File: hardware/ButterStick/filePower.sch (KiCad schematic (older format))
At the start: 28 parts, among them U1 TLV725P, U15 XCL206, U8 TLV718P, U9 TLV711P

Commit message: Updated PCB. Routed all SYZYGY signals needed from the FPGA.
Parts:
- added C1: C, pkl_dipol:C_0402, symbol Device:C
- added C2: 1uF, pkl_dipol:C_0402, symbol Device:C
- added C24: 3.3n, pkl_dipol:C_0402, symbol Device:C
- added C38: 100n, pkl_dipol:C_0402, symbol Device:C
- added C39, C42: 22uF, pkl_dipol:C_0805, symbol Device:CP1
- added L2: L, Inductor_SMD:L_Taiyo-Yuden_MD-3030, symbol Device:L
- added R1, R2, R5: R, pkl_dipol:R_0402, symbol Device:R
- added U2: BD9D323QWZ, gkl_housings_dfn:UMMP008Z2020, symbol gkl_pmic:BD9D323QWZ
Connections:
- net labels added: DAC_PORT0, PORT0_VCCIO, VIN, VREG1_EN
- wire segments 134 -> 176
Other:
- moved on the sheet: C48, C49, U15

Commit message: Update schematic hieracy layout.
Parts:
- removed C1: C, pkl_dipol:C_0402, symbol Device:C
- removed C2: 1uF, pkl_dipol:C_0402, symbol Device:C
- removed C24: 3.3n, pkl_dipol:C_0402, symbol Device:C
- removed C38: 100n, pkl_dipol:C_0402, symbol Device:C
- removed C39, C42: 22uF, pkl_dipol:C_0805, symbol Device:CP1
- removed L2: L, Inductor_SMD:L_Taiyo-Yuden_MD-3030, symbol Device:L
- removed R1, R2, R5: R, pkl_dipol:R_0402, symbol Device:R
- removed U2: BD9D323QWZ, gkl_housings_dfn:UMMP008Z2020, symbol gkl_pmic:BD9D323QWZ
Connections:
- net labels removed: DAC_PORT0, PORT0_VCCIO, VIN, VREG1_EN
- wire segments 176 -> 134

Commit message: Routed all SYZYGY ports. Placed decoupling caps etc.
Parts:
- removed C12: 100nF, pkl_dipol:C_0402, symbol Device:C
- removed R27: 0R, Resistors_SMD:R_0603, symbol Device:R
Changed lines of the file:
@@
 $Descr A4 11693 8268
 encoding utf-8
-Sheet 7 13
+Sheet 7 14
 Title ""
 Date ""
@@
 	1    0    0    -1
 $EndComp
-$Comp
-L Device:C C?
-U 1 1 5BC5589D
-P 6850 4250
-AR Path="/5ABC9A87/5BC5589D" Ref="C?"  Part="1"
-AR Path="/5BBD18EA/5BC5589D" Ref="C12"  Part="1"
-F 0 "C12" H 6900 4350 50  0000 L CNN
-F 1 "100nF" H 6900 4150 50  0000 L CNN
-F 2 "pkl_dipol:C_0402" H 6888 4100 50  0001 C CNN
-F 3 "" H 6850 4250 50  0001 C CNN
-F 4 "1276-1002-1-ND" H 2000 -1700 50  0001 C CNN "SN-DK"
-F 5 "CL05B104KP5NNNC" H 2000 -1700 50  0001 C CNN "PN"
-	1    6850 4250
-	1    0    0    -1
-$EndComp
-Wire Wire Line
-	6850 4000 6850 4100
-Wire Wire Line
-	6850 4400 6850 4500
-$Comp
-L gkl_power:GND #PWR?
-U 1 1 5BC558A8
-P 6850 4500
-AR Path="/5ABC9A87/5BC558A8" Ref="#PWR?"  Part="1"
-AR Path="/5BBD18EA/5BC558A8" Ref="#PWR0108"  Part="1"
-F 0 "#PWR0108" H 6850 4250 50  0001 C CNN
-F 1 "GND" H 6853 4374 50  0000 C CNN
-F 2 "" H 6750 4150 50  0001 C CNN
-F 3 "" H 6850 4500 50  0001 C CNN
-	1    6850 4500
-	1    0    0    -1
-$EndComp
-$Comp
-L gkl_power:+3V3 #PWR0218
-U 1 1 5BC5CBA2
-P 5950 3800
-F 0 "#PWR0218" H 5950 3650 50  0001 C CNN
-F 1 "+3V3" H 5953 3951 50  0000 C CNN
-F 2 "" H 5950 3800 50  0001 C CNN
-F 3 "" H 5950 3800 50  0001 C CNN
-	1    5950 3800
-	1    0    0    -1
-$EndComp
-$Comp
-L Device:R R27
-U 1 1 5BC5CBF3
-P 6400 4000
-F 0 "R27" V 6300 3900 50  0000 C CNN
-F 1 "0R" V 6300 4100 50  0000 C CNN
-F 2 "Resistors_SMD:R_0603" V 6330 4000 50  0001 C CNN
-F 3 "~" H 6400 4000 50  0001 C CNN
-F 4 "ERJ-3GEY0R00V" H 0   0   50  0001 C CNN "PN"
-F 5 "P0.0GCT-ND" H 0   0   50  0001 C CNN "SN-DK"
-	1    6400 4000
-	0    -1   -1   0
-$EndComp
-Text GLabel 6950 4000 2    60   Input ~ 0
-VCCIO6
-Wire Wire Line
-	6950 4000 6850 4000
-Connection ~ 6850 4000
-Wire Wire Line
-	6550 4000 6850 4000
-Wire Wire Line
-	6250 4000 5950 4000
-Wire Wire Line
-	5950 4000 5950 3800
 $EndSCHEMATC

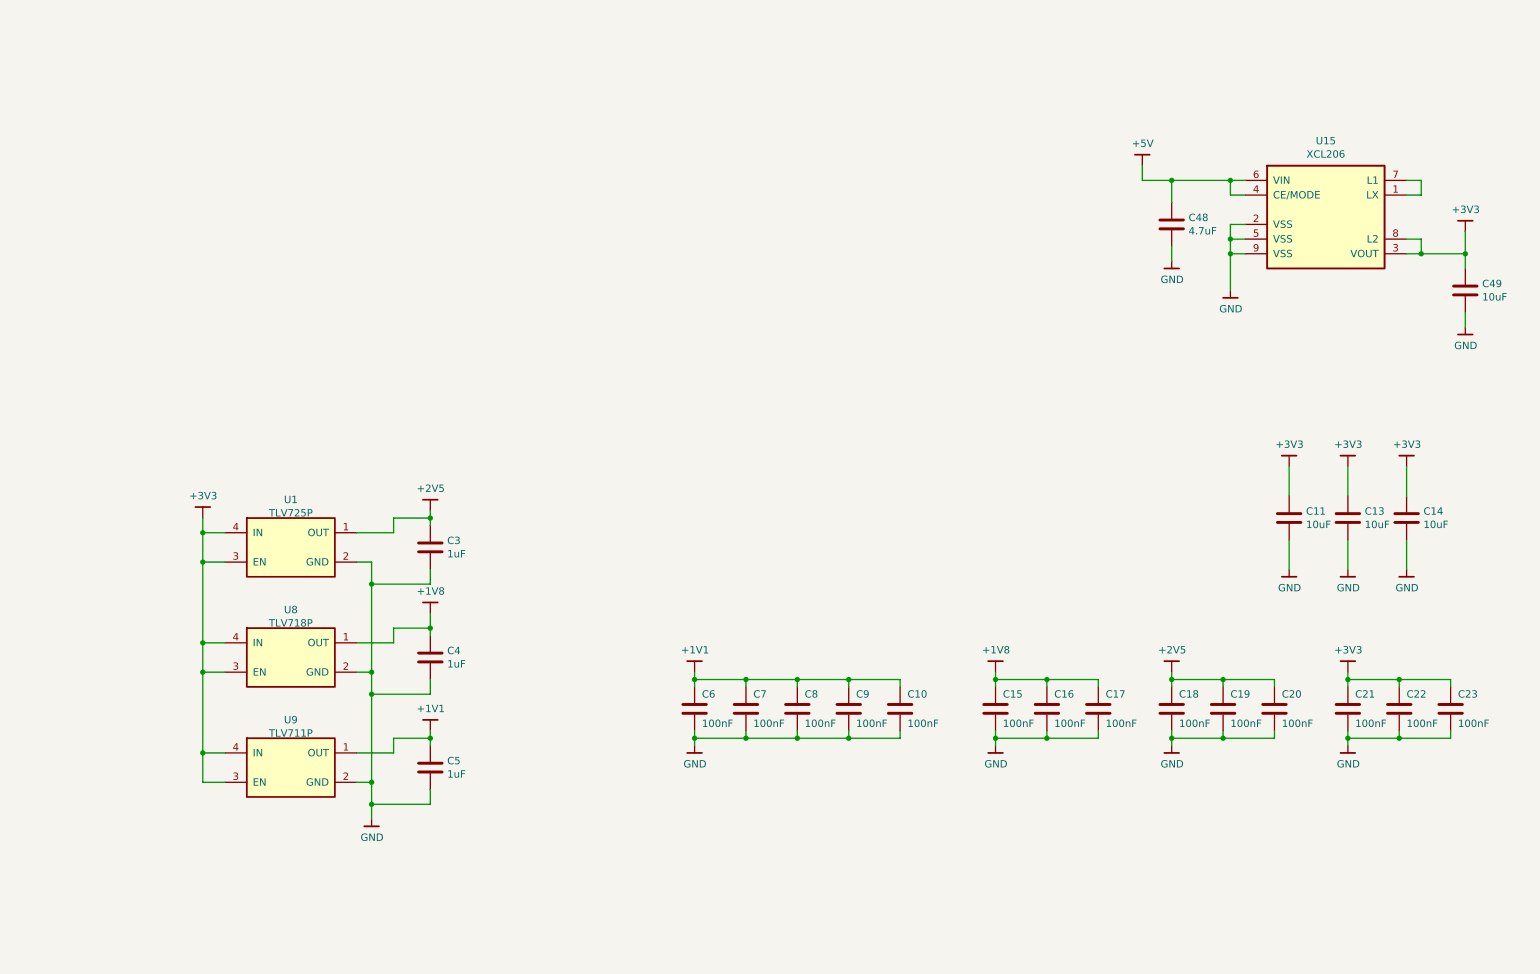
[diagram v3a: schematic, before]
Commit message: Added ESD on SD card signals.
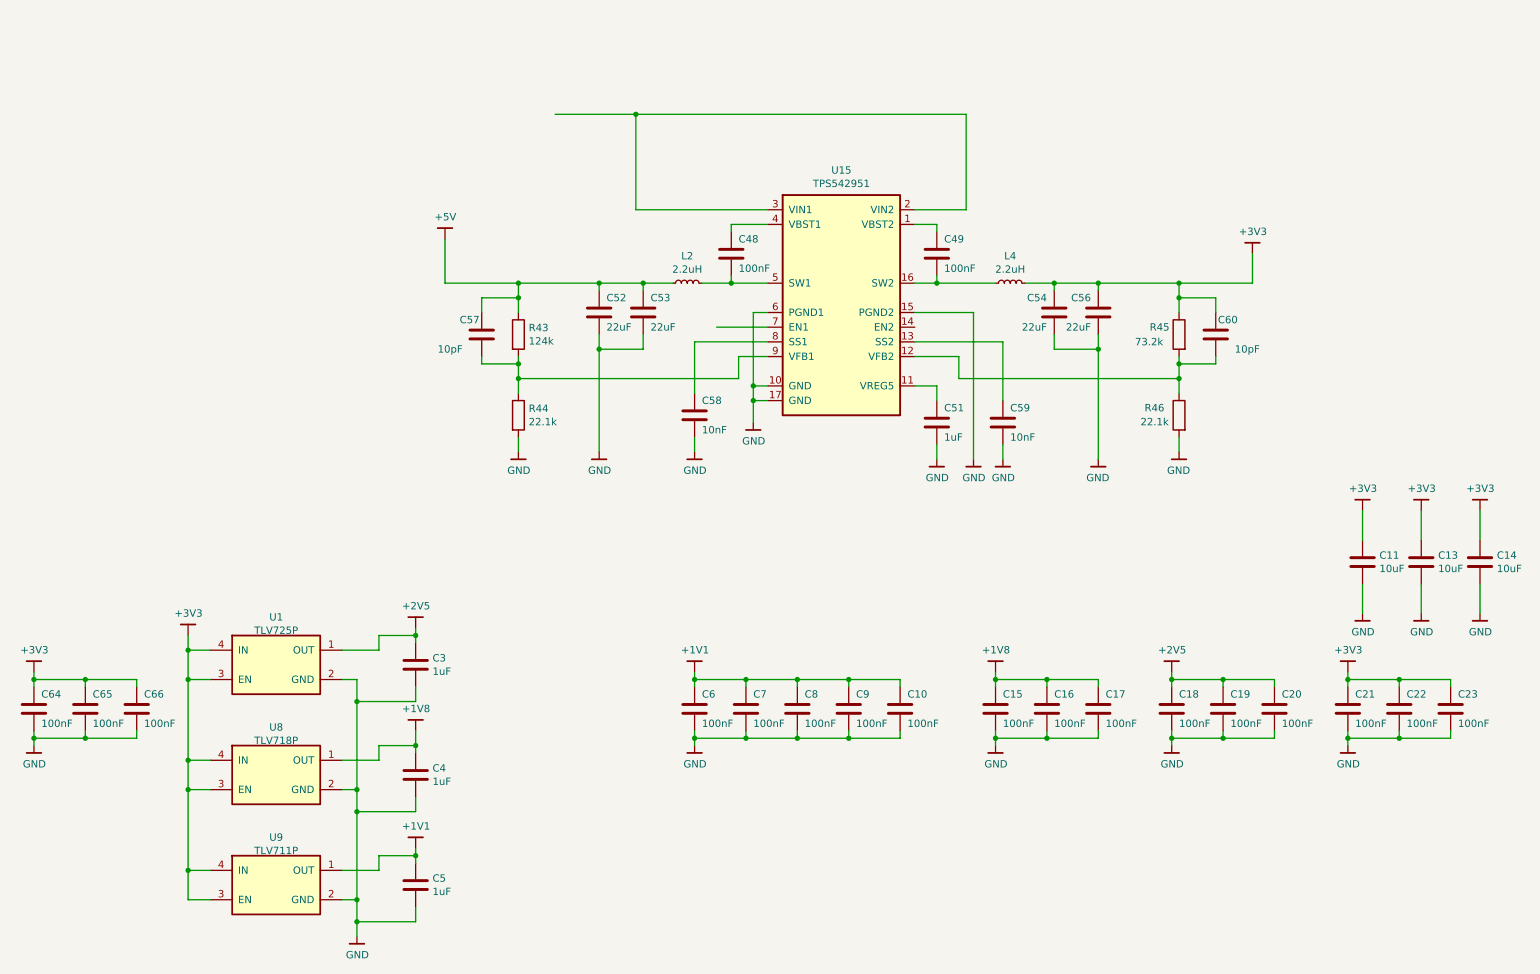
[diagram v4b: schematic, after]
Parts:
- removed U15: XCL206, bosonFrameGrabber:CL-2025, symbol gkl_pmic:XCL206
- added C51: 1uF, pkl_dipol:C_0402, symbol Device:C
- added C52, C53, C54, C56: 22uF, pkl_dipol:C_0805, symbol Device:C
- added C57, C60: 10pF, pkl_dipol:C_0402, symbol Device:C
- added C58, C59: 10nF, pkl_dipol:C_0402, symbol Device:C
- added C64, C65, C66: 100nF, pkl_dipol:C_0402, symbol Device:C
- added L2, L4: 2.2uH, Inductor_SMD:L_Taiyo-Yuden_MD-5050, symbol Device:L_Small
- added R43: 124k, pkl_dipol:R_0402, symbol Device:R
- added R44, R46: 22.1k, pkl_dipol:R_0402, symbol Device:R
- added R45: 73.2k, pkl_dipol:R_0402, symbol Device:R
- added U15: TPS542951, Package_DFN_QFN:QFN-16-1EP_4x4mm_P0.65mm_EP2.7x2.7mm_ThermalVias, symbol gkl_pmic:TPS542951
- C48: value 4.7uF -> 100nF; footprint pkl_dipol:C_0603 -> pkl_dipol:C_0402; PN CL10A475KP8NNNC -> CL05B104KP5NNNC; SN-DK 1276-1044-1-ND -> 1276-1002-1-ND
- C49: value 10uF -> 100nF; footprint pkl_dipol:C_0603 -> pkl_dipol:C_0402; PN C1608X5R1A106K080AC -> CL05B104KP5NNNC; SN-DK 445-7486-1-ND -> 1276-1002-1-ND
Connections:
- net +3V3: now also C54.1, C56.1, C60.1, C64.1, C65.1, C66.1, L4.2, R45.1; no longer C49.1
- net +5V: now also C52.1, C53.1, C57.1, L2.1, R43.1; no longer C48.1
- net GND: now also C51.2, C52.2, C53.2, C54.2, C56.2, C58.2, C59.2, C64.2, C65.2, C66.2, R44.2, R46.2, U15.10 (GND), U15.15 (PGND2), U15.17 (GND), U15.6 (PGND1); no longer C48.2, C49.2
- new net: C49.1, U15.1 (VBST2)
- new net: C51.1, U15.11 (VREG5)
- new net: C60.2, R45.2, R46.1, U15.12 (VFB2)
- new net: C59.1, U15.13 (SS2)
- new net: C49.2, L4.1, U15.16 (SW2)
- new net: U15.2 (VIN2), U15.3 (VIN1)
- new net: C48.1, U15.4 (VBST1)
- new net: C48.2, L2.2, U15.5 (SW1)
- new net: C58.1, U15.8 (SS1)
- new net: C57.2, R43.2, R44.1, U15.9 (VFB1)
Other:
- moved on the sheet: C11, C13, C14, C3, C4, C5, U1, U8, U9

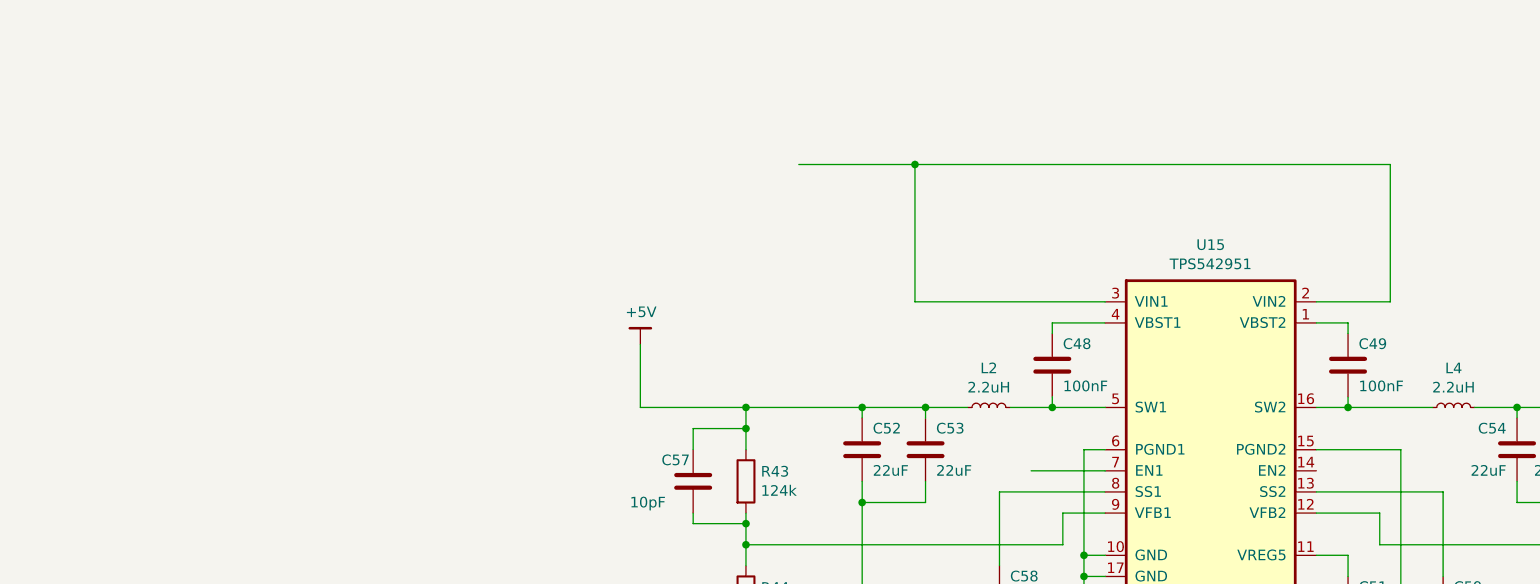
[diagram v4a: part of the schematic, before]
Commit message: Finished initial routing of PCB.. Most parts are finished.
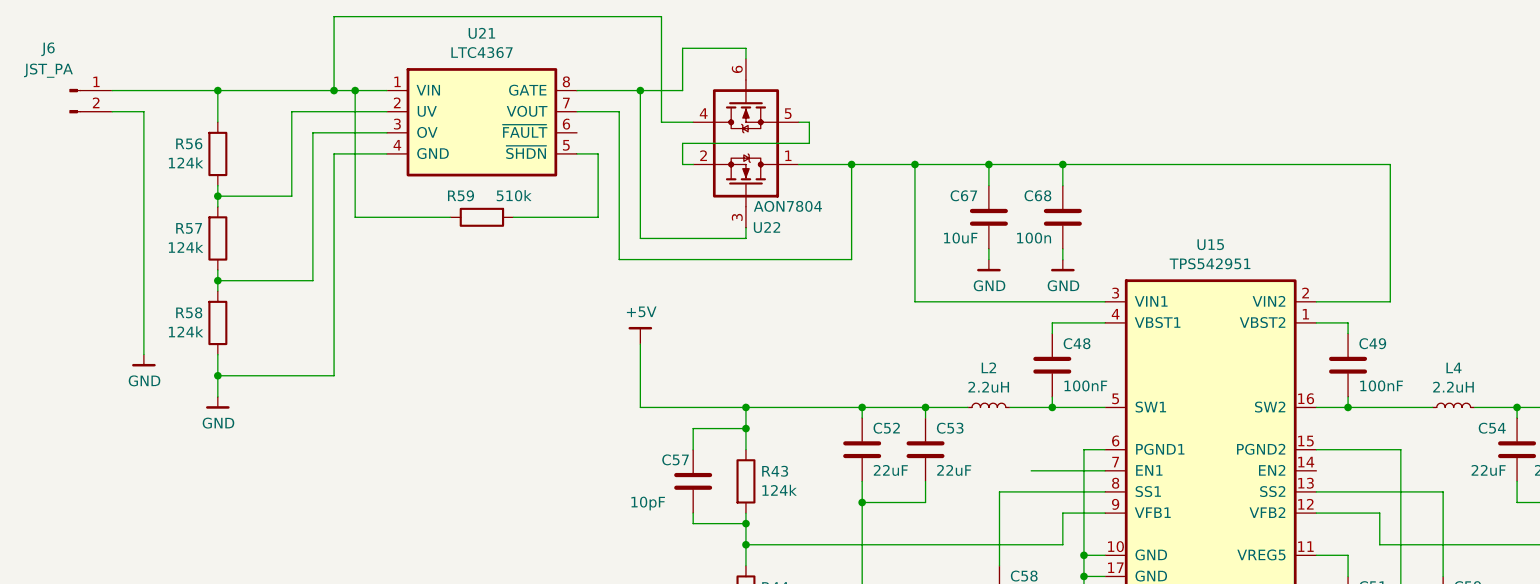
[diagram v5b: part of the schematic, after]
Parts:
- added C67: 10uF, pkl_dipol:C_0805, symbol Device:C
- added C68: 100n, pkl_dipol:C_0603, symbol Device:C
- added J6: JST_PA, symbol Connector:Conn_01x02_Male
- added R56, R57, R58: 124k, pkl_dipol:R_0402, symbol Device:R
- added R59: 510k, pkl_dipol:R_0402, symbol Device:R
- added U21: LTC4367, Package_SO:MSOP-8_3x3mm_P0.65mm, symbol gkl_pmic:LTC4367
- added U22: AON7804, gkl_housings_dfn:DFN3X3_8L_EP2_P, symbol gkl_mosfet:AON7804
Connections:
- net GND: now also C67.2, C68.2, J6.2 (Pin_2), R58.1, U21.4 (GND)
- net at U15.2 (VIN2), U15.3 (VIN1): now also C67.1, C68.1, U21.7 (VOUT), U22.1 (D)
- new net: J6.1 (Pin_1), R56.2, R59.1, U21.1 (VIN), U22.4 (D)
- new net: R56.1, R57.2, U21.2 (UV)
- new net: R57.1, R58.2, U21.3 (OV)
- new net: R59.2, U21.5 (~SHDN)
- new net: U21.8 (GATE), U22.3 (G), U22.6 (G)
- new net: U22.2 (S), U22.5 (S)

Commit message: Update KiCad PCB.
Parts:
- added C69, C70: 10uF, pkl_dipol:C_0805, symbol Device:C
- added R61, R62: 10k, pkl_dipol:R_0402, symbol Device:R
- J6: footprint (none) -> gkl_conn:SB02B-PASK-2
- L2, L4: MFG (none) -> Taiyo Yuden; PN (none) -> NR5040T2R2N
- U15: MFG (none) -> Texas Instruments; PN (none) -> TPS542951RSAR
- U21: MFG (none) -> Linear Technology/Analog Devices; PN (none) -> LTC4367IMS8-1#PBF
- U22: MFG (none) -> Alpha & Omega Semiconductor Inc.; PN (none) -> AON7804
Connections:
- net GND: now also C69.2, C70.2
- net EN2: now reaches U15.14 (EN2)
- net EN2: now also R62.1
- net at C67.1, C68.1, U15.2 (VIN2)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: now also C69.1, C70.1, R61.2, R62.2
- net EN1: now reaches U15.7 (EN1)
- net EN1: now also R61.1
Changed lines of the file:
@@
 F 2 "Package_DFN_QFN:QFN-16-1EP_4x4mm_P0.65mm_EP2.7x2.7mm_ThermalVias" H 6350 2850 50  0001 C CNN
 F 3 "" H 6350 2850 50  0001 C CNN
+F 4 "Texas Instruments" H 6350 2400 50  0001 C CNN "MFG"
+F 5 "TPS542951RSAR" H 6350 2400 50  0001 C CNN "PN"
 	1    6350 2400
 	1    0    0    -1
@@
 	7200 2100 7200 1450
 Wire Wire Line
-	7200 1450 5650 1450
+	7200 1450 7000 1450
 Connection ~ 4950 1450
 $Comp
@@
 F 2 "Inductor_SMD:L_Taiyo-Yuden_MD-5050" H 5300 2600 50  0001 C CNN
 F 3 "~" H 5300 2600 50  0001 C CNN
+F 4 "Taiyo Yuden" H 0   0   50  0001 C CNN "MFG"
+F 5 "NR5040T2R2N" H 0   0   50  0001 C CNN "PN"
 	1    5300 2600
 	0    -1   -1   0
@@
 F 2 "Inductor_SMD:L_Taiyo-Yuden_MD-5050" H 7500 2600 50  0001 C CNN
 F 3 "~" H 7500 2600 50  0001 C CNN
+F 4 "Taiyo Yuden" H 0   0   50  0001 C CNN "MFG"
+F 5 "NR5040T2R2N" H 0   0   50  0001 C CNN "PN"
 	1    7500 2600
 	0    -1   -1   0
@@
 F 2 "Package_SO:MSOP-8_3x3mm_P0.65mm" H 2900 1550 50  0001 C CNN
 F 3 "" H 2900 1550 50  0001 C CNN
+F 4 "Linear Technology/Analog Devices" H 2900 1250 50  0001 C CNN "MFG"
+F 5 "LTC4367IMS8-1#PBF" H 2900 1250 50  0001 C CNN "PN"
 	1    2900 1250
 	1    0    0    -1
@@
 F 0 "J6" H 850 1300 50  0000 C CNN
 F 1 "JST_PA" H 850 1200 50  0000 C CNN
-F 2 "" H 950 1100 50  0001 C CNN
+F 2 "gkl_conn:SB02B-PASK-2" H 950 1100 50  0001 C CNN
 F 3 "~" H 950 1100 50  0001 C CNN
 	1    950  1100
@@
 F 2 "gkl_housings_dfn:DFN3X3_8L_EP2_P" H 3700 1550 50  0001 C CNN
 F 3 "" H 3700 1550 50  0001 C CNN
+F 4 "Alpha & Omega Semiconductor Inc." H 4150 1350 50  0001 C CNN "MFG"
+F 5 "AON7804" H 4150 1350 50  0001 C CNN "PN"
 	1    4150 1350
 	0    1    -1   0
@@
 	1    0    0    -1
 $EndComp
+Wire Wire Line
+	6850 2900 7400 2900
+Text Label 7400 2900 0    50   ~ 0
+EN2
+Text Label 5500 2900 0    50   ~ 0
+EN1
+$Comp
+L Device:C C?
+U 1 1 5CF123E9
+P 7450 1700
+AR Path="/5ABC9A87/5CF123E9" Ref="C?"  Part="1"
+AR Path="/5BBD18EA/5CF123E9" Ref="C69"  Part="1"
+F 0 "C69" H 7500 1800 50  0000 L CNN
+F 1 "10uF" H 7500 1600 50  0000 L CNN
+F 2 "pkl_dipol:C_0805" H 7488 1550 50  0001 C CNN
+F 3 "" H 7450 1700 50  0001 C CNN
+F 4 "1276-1002-1-ND" H 2950 -5250 50  0001 C CNN "SN-DK"
+F 5 "CL05B104KP5NNNC" H 2950 -5250 50  0001 C CNN "PN"
+	1    7450 1700
+	-1   0    0    -1
+$EndComp
+$Comp
+L gkl_power:GND #PWR0267
+U 1 1 5CF123EF
+P 7450 1900
+F 0 "#PWR0267" H 7450 1650 50  0001 C CNN
+F 1 "GND" H 7453 1774 50  0000 C CNN
+F 2 "" H 7350 1550 50  0001 C CNN
+F 3 "" H 7450 1900 50  0001 C CNN
+	1    7450 1900
+	1    0    0    -1
+$EndComp
+Wire Wire Line
+	7450 1900 7450 1850
+Wire Wire Line
+	7450 1550 7450 1450
+$Comp
+L Device:C C?
+U 1 1 5CF256A8
+P 7750 1700
+AR Path="/5ABC9A87/5CF256A8" Ref="C?"  Part="1"
+AR Path="/5BBD18EA/5CF256A8" Ref="C70"  Part="1"
+F 0 "C70" H 7800 1800 50  0000 L CNN
+F 1 "10uF" H 7800 1600 50  0000 L CNN
+F 2 "pkl_dipol:C_0805" H 7788 1550 50  0001 C CNN
+F 3 "" H 7750 1700 50  0001 C CNN
+F 4 "1276-1002-1-ND" H 3250 -5250 50  0001 C CNN "SN-DK"
+F 5 "CL05B104KP5NNNC" H 3250 -5250 50  0001 C CNN "PN"
+	1    7750 1700
+	-1   0    0    -1
+$EndComp
+$Comp
+L gkl_power:GND #PWR0268
+U 1 1 5CF256AE
+P 7750 1900
+F 0 "#PWR0268" H 7750 1650 50  0001 C CNN
+F 1 "GND" H 7753 1774 50  0000 C CNN
+F 2 "" H 7650 1550 50  0001 C CNN
+F 3 "" H 7750 1900 50  0001 C CNN
+	1    7750 1900
+	1    0    0    -1
+$EndComp
+Wire Wire Line
+	7750 1900 7750 1850
+Wire Wire Line
+	7750 1550 7750 1450
+Wire Wire Line
+	7200 1450 7450 1450
+Connection ~ 7200 1450
+Wire Wire Line
+	7450 1450 7750 1450
+Connection ~ 7450 1450
+Text Label 8700 1150 0    50   ~ 0
+EN1
+Text Label 8700 1300 0    50   ~ 0
+EN2
+$Comp
+L Device:R R61
+U 1 1 5C8641F5
+P 8300 1150
+F 0 "R61" V 8400 1100 50  0000 R CNN
+F 1 "10k" V 8400 1300 50  0000 R CNN
+F 2 "pkl_dipol:R_0402" V 8230 1150 50  0001 C CNN
+F 3 "~" H 8300 1150 50  0001 C CNN
+	1    8300 1150
+	0    1    -1   0
+$EndComp
+Wire Wire Line
+	8450 1150 8700 1150
+Wire Wire Line
+	8150 1150 7950 1150
+Wire Wire Line
+	7000 1150 7000 1450
+Connection ~ 7000 1450
+Wire Wire Line
+	7000 1450 5650 1450
+$Comp
+L Device:R R62
+U 1 1 5C88BD7C
+P 8300 1300
+F 0 "R62" V 8200 1200 50  0000 R CNN
+F 1 "10k" V 8200 1500 50  0000 R CNN
+F 2 "pkl_dipol:R_0402" V 8230 1300 50  0001 C CNN
+F 3 "~" H 8300 1300 50  0001 C CNN
+	1    8300 1300
+	0    1    -1   0
+$EndComp
+Wire Wire Line
+	8450 1300 8700 1300
+Wire Wire Line
+	8150 1300 7950 1300
+Wire Wire Line
+	7950 1300 7950 1150
+Connection ~ 7950 1150
+Wire Wire Line
+	7950 1150 7000 1150
 $EndSCHEMATC
